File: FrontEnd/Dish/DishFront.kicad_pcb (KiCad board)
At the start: 2 copper layers, 131.3 x 54.4 mm, 204 parts, among them P1 BNC, U1 PMA-545G1_Amp, U10 HSWA2-30DR_switch, U11 HSWA2-30DR_switch, U12 SN74AUP1T86_Schmitt_XOR, U13 SN74AUP1T86_Schmitt_XOR, U14 SN74AUP1T86_Schmitt_XOR, U15 SN74AUP1T86_Schmitt_XOR, U16 SN74AUP1T86_Schmitt_XOR, U17 SN74AUP1T86_Schmitt_XOR, U18 SN74AUP1T86_Schmitt_XOR, U19 SN74AUP1T86_Schmitt_XOR, U2 HSWA2-30DR_switch, U20 SN74AUP1T86_Schmitt_XOR, U21 SN74AUP1T86_Schmitt_XOR, U22 SN74AUP1T86_Schmitt_XOR, U23 SN74AUP1T86_Schmitt_XOR, U24 MC_DBTC-17-5_Coupler, U25 PSA4-5043_Amp, U26 MC_TCBT-2R5G_BiasT, U3 HSWA2-30DR_switch, U4 HSWA2-30DR_switch, U5 MC_HQ1157_Bandpass, U6 MC_HQ1157_Bandpass, U7 MC_HQ1157_Bandpass, U8 MC_HQ1157_Bandpass, U9 HSWA2-30DR_switch

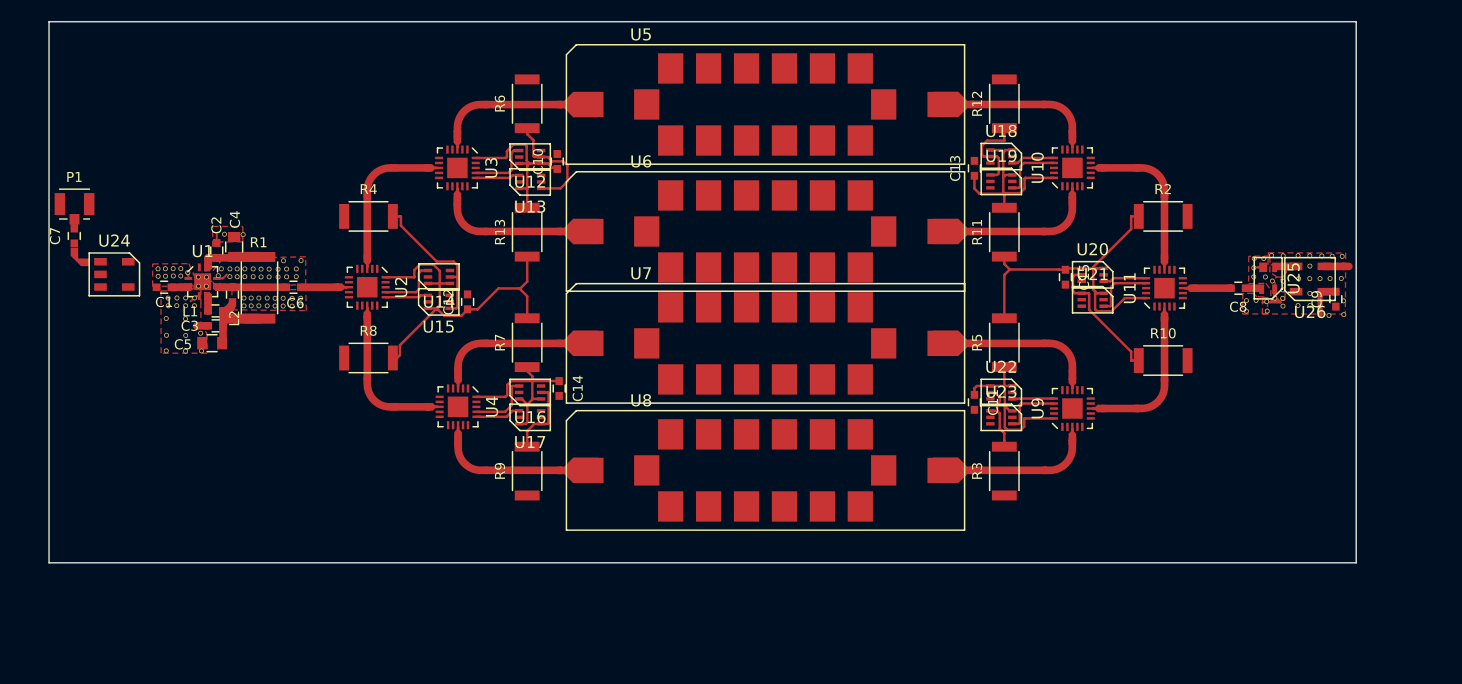
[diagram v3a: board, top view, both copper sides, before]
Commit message: [Fixed] Minicircuits Bias Tee pad numbering issue; [Added] SMA Edge mount part
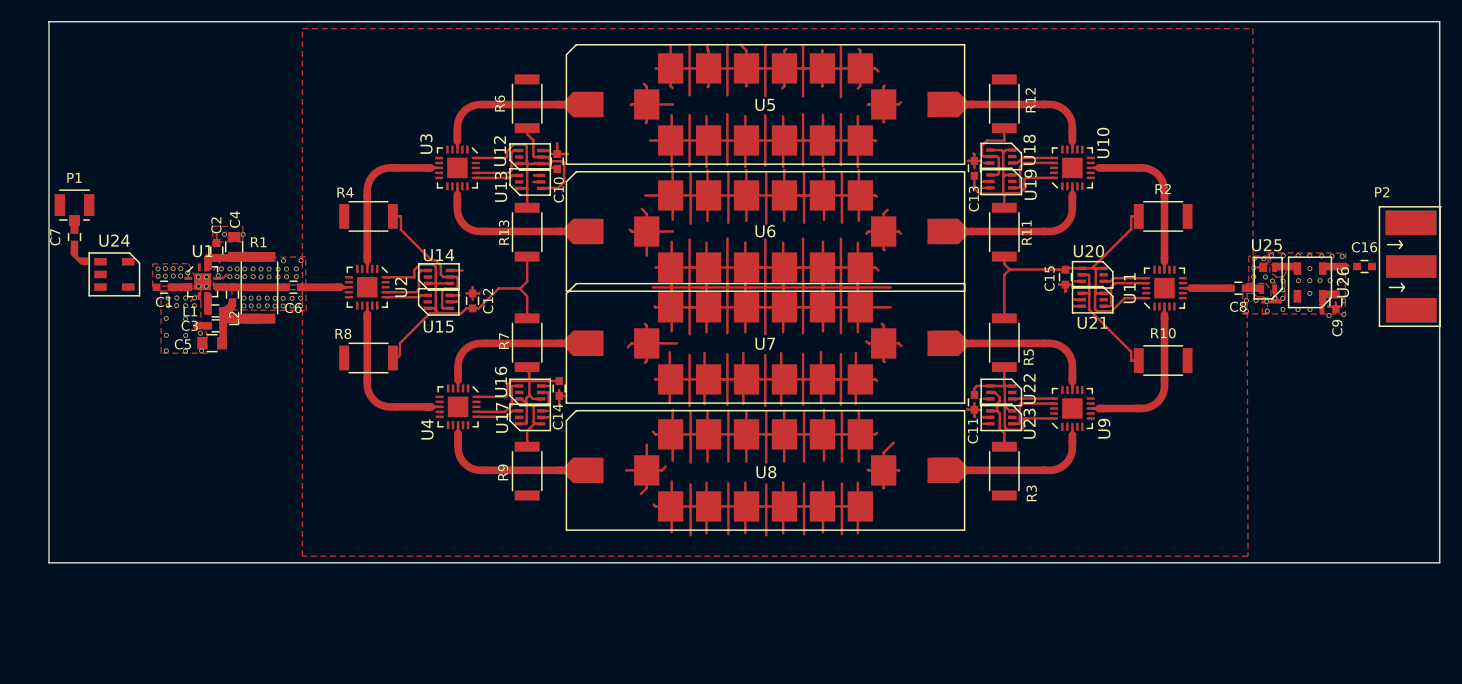
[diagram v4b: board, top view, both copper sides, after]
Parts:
- added ?: , Minicircuits:40mil-30mil, F.Cu at (85.1, 55.9)
- added C16: 100pF, Capacitors_SMD:C_0603, F.Cu at (214.7, 59.9)
- added P2: BNC, DigitalLogic:SMA_EDGE, F.Cu at (219.4, 59.9)
- moved C12 0.51 mm to (125.1, 63.4)
- moved ? 0.40 mm to (208.0, 64.2)
- moved ? 0.40 mm to (209.2, 64.2)
- moved U26 0.34 mm to (209.2, 61.5), turned to 180 degrees
- moved ? 0.32 mm to (206.5, 64.2)
- moved C9 0.27 mm to (211.8, 63.5)
- moved ? 0.24 mm to (209.2, 60.1)
- moved ? 0.20 mm to (212.4, 61.3)
- moved ? 0.20 mm to (211.2, 61.3)
- moved ? 0.20 mm to (208.1, 61.3)
- moved ? 0.20 mm to (210.2, 61.3)
- moved ? 0.20 mm to (209.2, 61.3)
- moved ? 0.12 mm to (85.5, 59.0)
- moved C7 0.11 mm to (85.1, 56.9)
- moved P1 0.10 mm to (85.1, 53.7)
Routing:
- net (no net): track 0.00 -> 382.9 mm
- net GND: track 7.68 -> 373.5 mm
- net Net-(U26-Pad2): track 2.64 -> 0.00 mm
- net Net-(C16-Pad1): track 0.00 -> 2.20 mm
- net +5V: track 12.3 -> 11.6 mm
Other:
- board size 131.3 x 54.4 mm -> 139.7 x 54.4 mm
